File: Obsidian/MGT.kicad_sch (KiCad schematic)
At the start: 1 part, among them U1 XC7A35T-CSG325

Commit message: update with available components on LCSC
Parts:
- U1: FT Rotation Offset (none) -> 0; LCSC (none) -> C1521749
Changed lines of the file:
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@@
+			)
+		)
+		(property "FT Rotation Offset" "0"
+			(at 160.02 80.01 0)
+			(effects
+				(font
+					(size 1.27 1.27)
+				)
+				(hide yes)
+			)
+		)
+		(property "LCSC" "C1521749"
+			(at 160.02 80.01 0)
+			(effects
+				(font
+					(size 1.27 1.27)
+				)
+				(hide yes)
 			)
 		)

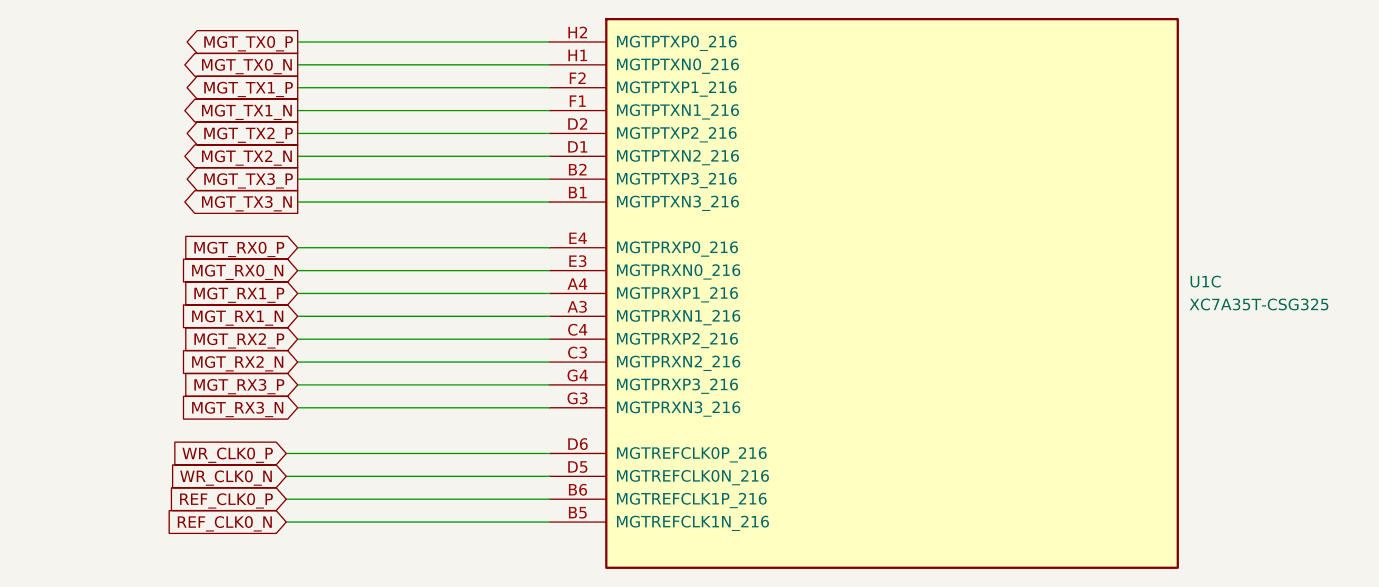
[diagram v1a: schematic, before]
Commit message: replacing global label with hierarchical label
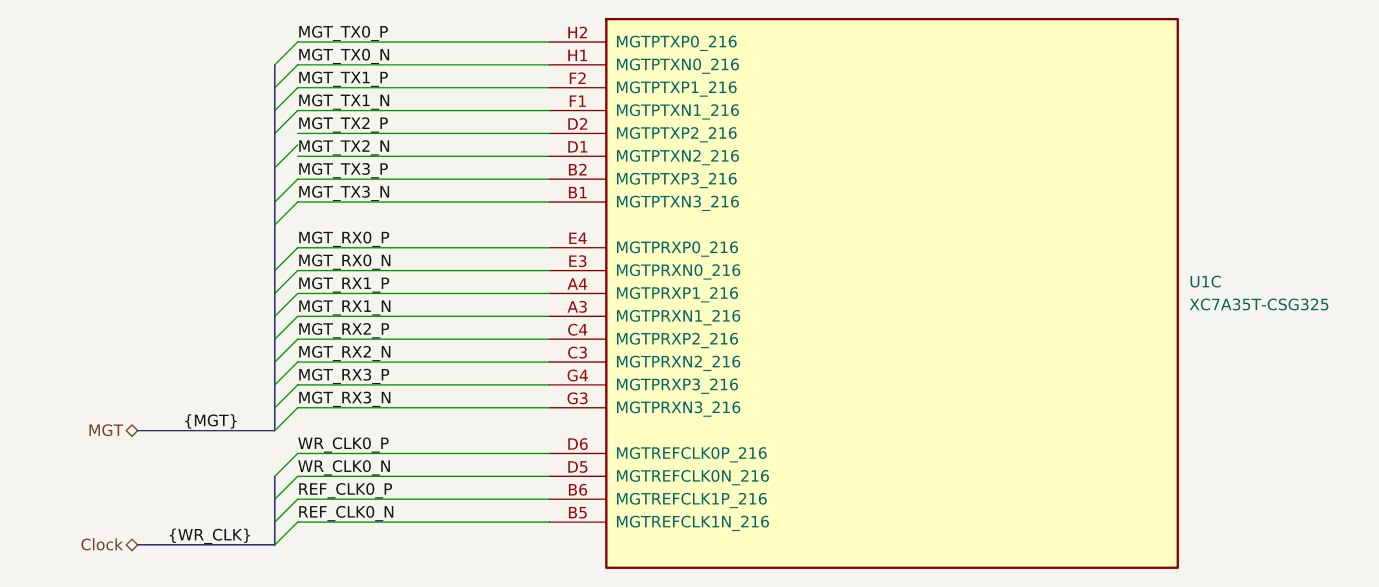
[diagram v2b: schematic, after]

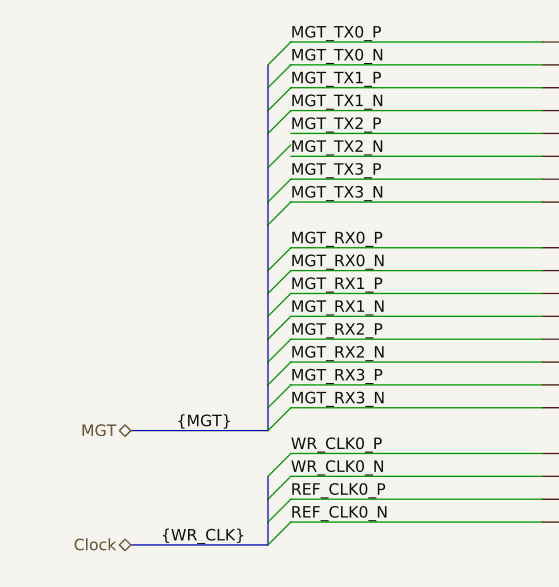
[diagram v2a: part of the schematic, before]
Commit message: Adding symbol library
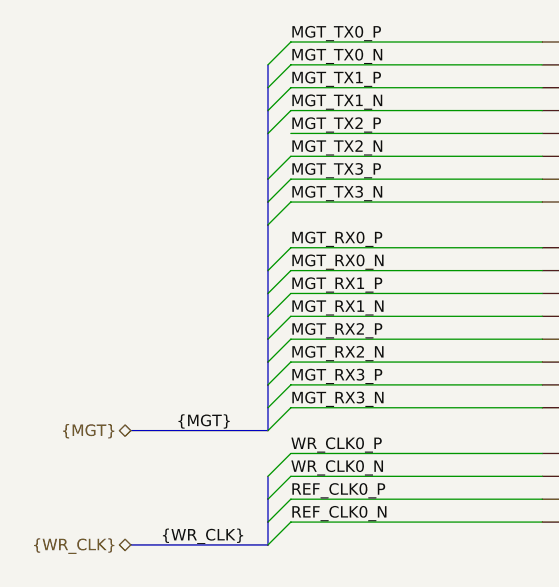
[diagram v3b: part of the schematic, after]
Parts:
- U1: symbol FPGA_Xilinx_Artix7:XC7A35T-CSG325 -> Library_Symbol:XC7A35T-CSG325
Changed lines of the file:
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@@
 	)
 	(bus_entry
-		(at 91.44 66.04)
+		(at 91.44 67.31)
 		(size 2.54 -2.54)
 		(stroke
@@
 	(bus
 		(pts
-			(xy 91.44 66.04) (xy 91.44 69.85)
+			(xy 91.44 67.31) (xy 91.44 69.85)
 		)
 		(stroke
@@
 	(bus
 		(pts
-			(xy 91.44 62.23) (xy 91.44 66.04)
+			(xy 91.44 62.23) (xy 91.44 67.31)
 		)
 		(stroke
@@
 		)
 	)
-	(hierarchical_label "MGT"
+	(hierarchical_label "{MGT}"
 		(shape bidirectional)
 		(at 76.2 95.25 180)
@@
 		)
 	)
-	(hierarchical_label "Clock"
+	(hierarchical_label "{WR_CLK}"
 		(shape bidirectional)
 		(at 76.2 107.95 180)
@@
 	)
 	(symbol
-		(lib_id "FPGA_Xilinx_Artix7:XC7A35T-CSG325")
+		(lib_id "Library_Symbol:XC7A35T-CSG325")
 		(at 160.02 80.01 0)
 		(unit 3)

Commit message: Correct Schematic errors
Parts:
- U1: footprint Package_BGA:Xilinx_CSG325 -> Footprint:Xilinx_CSG325
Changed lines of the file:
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@@
 			)
 		)
-		(property "Footprint" "Package_BGA:Xilinx_CSG325"
+		(property "Footprint" "Footprint:Xilinx_CSG325"
 			(at 160.02 80.01 0)
 			(effects

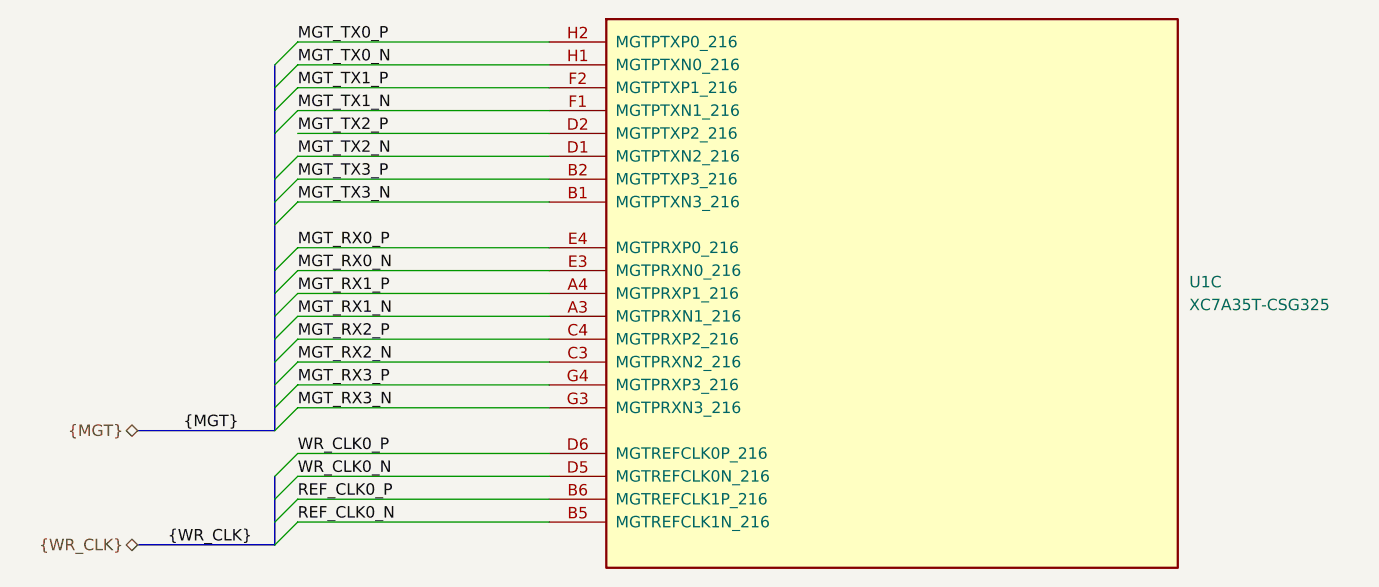
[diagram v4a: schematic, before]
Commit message: Cleanup of the schematic
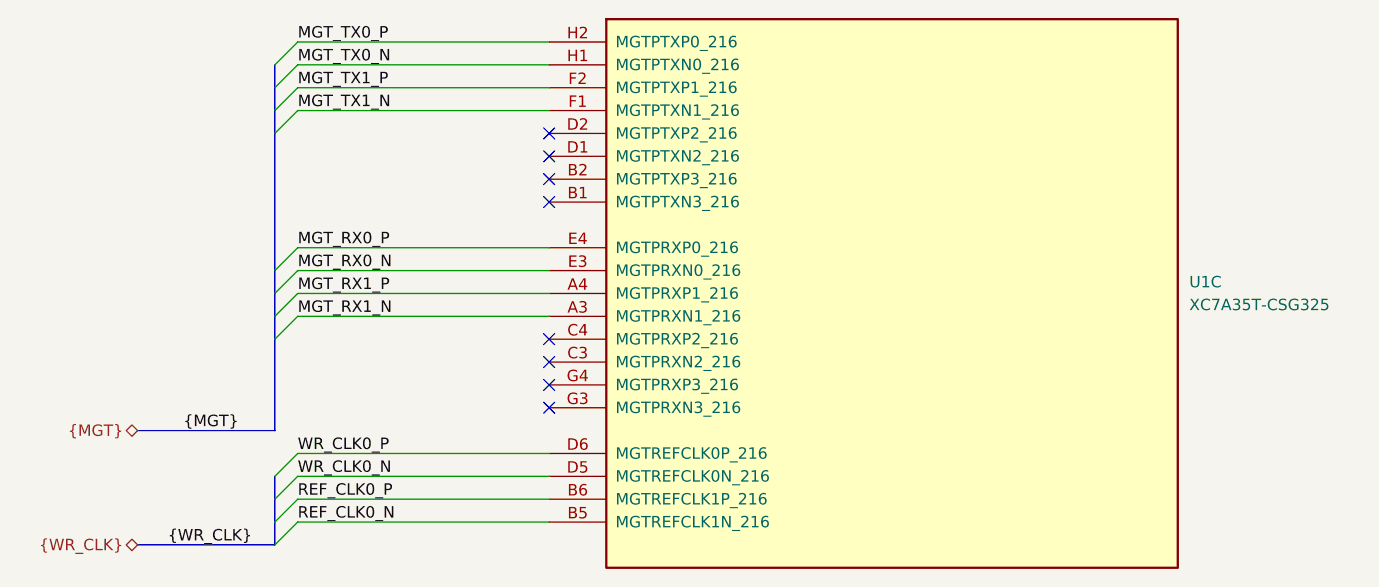
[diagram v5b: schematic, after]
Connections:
- net MGT_RX2_N: no longer names the net of U1.C3 (MGTPRXN2_216)
- net MGT_RX2_P: no longer names the net of U1.C4 (MGTPRXP2_216)
- net MGT_RX3_N: no longer names the net of U1.G3 (MGTPRXN3_216)
- net MGT_RX3_P: no longer names the net of U1.G4 (MGTPRXP3_216)
- net MGT_TX2_N: no longer names the net of U1.D1 (MGTPTXN2_216)
- net MGT_TX2_P: no longer names the net of U1.D2 (MGTPTXP2_216)
- net MGT_TX3_N: no longer names the net of U1.B1 (MGTPTXN3_216)
- net MGT_TX3_P: no longer names the net of U1.B2 (MGTPTXP3_216)
- no-connect marks 0 -> 8

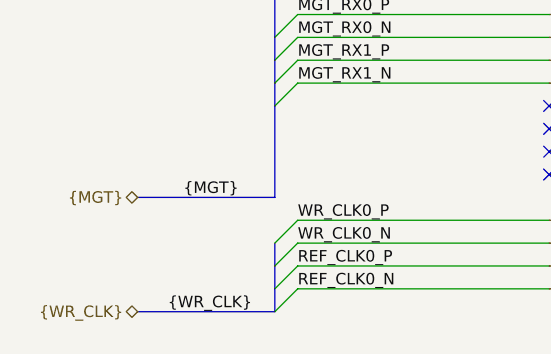
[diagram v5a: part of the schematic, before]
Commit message: Separating auxiliary clock from WR clock
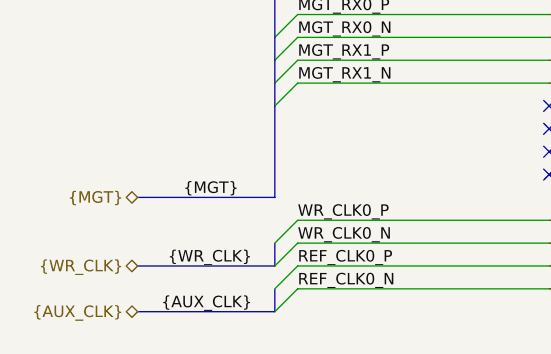
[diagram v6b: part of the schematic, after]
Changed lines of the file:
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@@
-	(bus
-		(pts
-			(xy 91.44 100.33) (xy 91.44 102.87)
-		)
-		(stroke
-			(width 0)
-			(type default)
-		)
-	)
 	(bus
 		(pts
@@
 	(bus
 		(pts
+			(xy 76.2 107.95) (xy 91.44 107.95)
+		)
+		(stroke
+			(width 0)
+			(type default)
+		)
+	)
+	(bus
+		(pts
 			(xy 91.44 82.55) (xy 91.44 85.09)
 		)
@@
 		)
 	)
-	(bus
-		(pts
-			(xy 76.2 107.95) (xy 91.44 107.95)
-		)
-		(stroke
-			(width 0)
-			(type default)
-		)
-	)
 	(wire
 		(pts
@@
 	(bus
 		(pts
+			(xy 91.44 102.87) (xy 91.44 100.33)
+		)
+		(stroke
+			(width 0)
+			(type default)
+		)
+	)
+	(bus
+		(pts
 			(xy 91.44 85.09) (xy 91.44 95.25)
 		)
@@
 		)
 	)
+	(bus
+		(pts
+			(xy 76.2 102.87) (xy 91.44 102.87)
+		)
+		(stroke
+			(width 0)
+			(type default)
+		)
+	)
 	(wire
 		(pts
@@
 	(bus
 		(pts
-			(xy 91.44 102.87) (xy 91.44 105.41)
+			(xy 91.44 107.95) (xy 91.44 105.41)
 		)
 		(stroke
@@
 		(pts
 			(xy 91.44 77.47) (xy 91.44 80.01)
-		)
-		(stroke
-			(width 0)
-			(type default)
-		)
-	)
-	(bus
-		(pts
-			(xy 91.44 107.95) (xy 91.44 105.41)
 		)
 		(stroke
@@
 		)
 	)
+	(label "{AUX_CLK}"
+		(at 88.9 107.95 180)
+		(effects
+			(font
+				(size 1.27 1.27)
+			)
+			(justify right bottom)
+		)
+	)
 	(label "MGT_RX0_P"
 		(at 93.98 74.93 0)
@@
 		)
 	)
-	(label "{WR_CLK}"
-		(at 88.9 107.95 180)
-		(effects
-			(font
-				(size 1.27 1.27)
-			)
-			(justify right bottom)
-		)
-	)
 	(label "MGT_TX1_P"
 		(at 93.98 57.15 0)
@@
 			)
 			(justify left bottom)
+		)
+	)
+	(label "{WR_CLK}"
+		(at 88.9 102.87 180)
+		(effects
+			(font
+				(size 1.27 1.27)
+			)
+			(justify right bottom)
 		)
 	)
@@
 		)
 	)
+	(hierarchical_label "{AUX_CLK}"
+		(shape bidirectional)
+		(at 76.2 107.95 180)
+		(effects
+			(font
+				(size 1.27 1.27)
+			)
+			(justify right)
+		)
+	)
 	(hierarchical_label "{WR_CLK}"
 		(shape bidirectional)
-		(at 76.2 107.95 180)
-		(effects
-			(font
+		(at 76.2 102.87 180)
+		(effects
+			(font
